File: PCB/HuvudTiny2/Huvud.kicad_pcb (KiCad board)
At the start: 4 copper layers, 42 x 42 mm, 101 parts, among them J1 MOLEX Micro Fit 2x3, J2 DBG, J3 THERM, J4 FAN0, J5 FAN1, J6 Heater, J7 Endstop, J8 THERM, J9 STEPPER, Q1 AO3400A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

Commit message: Remove all traces this time for real.
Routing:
- net HEATER: track 24.9 -> 0.00 mm
- net ENDSTOP2: track 18.3 -> 0.00 mm
- net USBD-: track 16.6 -> 0.00 mm
- net USBD+: track 16.0 -> 0.00 mm
- net /ST_A2: track 14.7 -> 0.00 mm
- net VCC_IO: track 12.9 -> 0.00 mm
- net SDI: track 11.3 -> 0.00 mm
- net /ST_A1: track 10.6 -> 0.00 mm
- net FAN0: track 10.2 -> 0.00 mm
- net /ST_B1: track 9.78 -> 0.00 mm
- net /ST_B2: track 8.28 -> 0.00 mm
- net ENDSTOP1: track 7.13 -> 0.00 mm
- net THERM2: track 5.48 -> 0.00 mm
- net THERM1: track 4.98 -> 0.00 mm
- net NRST: track 3.83 -> 0.00 mm
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
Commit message: Stepper power routed.
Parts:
- moved C9 1.66 mm to (208.0, 129.3), turned to 0 degrees
- turned R24 to 0 degrees
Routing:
- net GND: track 0.00 -> 14.1 mm
- net ST_EN: track 0.00 -> 6.02 mm
- net Net-(C5-Pad1): track 0.00 -> 3.29 mm
- net /ST_B1: track 0.00 -> 3.20 mm
- net Net-(C5-Pad2): track 0.00 -> 2.71 mm
- net /ST_A1: track 0.00 -> 2.68 mm
- net /ST_A2: track 0.00 -> 2.15 mm
- net /ST_B2: track 0.00 -> 1.98 mm
- net Net-(C4-Pad1): track 0.00 -> 1.33 mm
- net BRB: track 0.00 -> 1.20 mm
- net BRA: track 0.00 -> 1.08 mm
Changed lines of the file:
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@@
   )
   (footprint "Capacitor_SMD:C_0402_1005Metric" (layer "F.Cu")
-    (at 206.6 128.4 180)
+    (at 208 129.3)
     (descr "Capacitor SMD 0402 (1005 Metric), square (rectangular) end terminal, IPC_7351 nominal, (Body size source: http://www.tortai-tech.com/upload/download/2011102023233369053.pdf), generated with kicad-footprint-generator")
     (tags "capacitor")
@@
     (fp_line (start -0.5 0.25) (end -0.5 -0.25) (layer "F.Fab") (width 0.1))
     (fp_line (start -0.5 -0.25) (end 0.5 -0.25) (layer "F.Fab") (width 0.1))
-    (pad "1" smd roundrect locked (at -0.485 0 180) (size 0.59 0.64) (layers "F.Cu" "F.Paste" "F.Mask") (roundrect_rratio 0.25)
+    (pad "1" smd roundrect locked (at -0.485 0) (size 0.59 0.64) (layers "F.Cu" "F.Paste" "F.Mask") (roundrect_rratio 0.25)
       (net 2 "GND") (pintype "passive"))
-    (pad "2" smd roundrect locked (at 0.485 0 180) (size 0.59 0.64) (layers "F.Cu" "F.Paste" "F.Mask") (roundrect_rratio 0.25)
+    (pad "2" smd roundrect locked (at 0.485 0) (size 0.59 0.64) (layers "F.Cu" "F.Paste" "F.Mask") (roundrect_rratio 0.25)
       (net 57 "VCC_IO") (pintype "passive"))
     (model "${KISYS3DMOD}/Capacitor_SMD.3dshapes/C_0402_1005Metric.wrl"
@@
   )
   (footprint "Resistor_SMD:R_0402_1005Metric" (layer "F.Cu")
-    (at 206.1 126.4 180)
+    (at 206.1 126.4)
     (descr "Resistor SMD 0402 (1005 Metric), square (rectangular) end terminal, IPC_7351 nominal, (Body size source: http://www.tortai-tech.com/upload/download/2011102023233369053.pdf), generated with kicad-footprint-generator")
     (tags "resistor")
@@
     (fp_line (start 0.5 -0.25) (end 0.5 0.25) (layer "F.Fab") (width 0.1))
     (fp_line (start 0.5 0.25) (end -0.5 0.25) (layer "F.Fab") (width 0.1))
-    (pad "1" smd roundrect locked (at -0.485 0 180) (size 0.59 0.64) (layers "F.Cu" "F.Paste" "F.Mask") (roundrect_rratio 0.25)
+    (pad "1" smd roundrect locked (at -0.485 0) (size 0.59 0.64) (layers "F.Cu" "F.Paste" "F.Mask") (roundrect_rratio 0.25)
       (net 2 "GND") (pintype "passive"))
-    (pad "2" smd roundrect locked (at 0.485 0 180) (size 0.59 0.64) (layers "F.Cu" "F.Paste" "F.Mask") (roundrect_rratio 0.25)
+    (pad "2" smd roundrect locked (at 0.485 0) (size 0.59 0.64) (layers "F.Cu" "F.Paste" "F.Mask") (roundrect_rratio 0.25)
       (net 33 "ST_UART_RX") (pintype "passive"))
     (model "${KISYS3DMOD}/Resistor_SMD.3dshapes/R_0402_1005Metric.wrl"
@@
     (style (thickness 0.15) (arrow_length 1.27) (text_position_mode 2) (extension_height 0.58642) (extension_offset 0) keep_text_aligned)
   )
+  (segment (start 208.8878 124.0878) (end 209.2 124.4) (width 0.2) (layer "F.Cu") (net 2))
+  (segment (start 210.887799 123.1248) (end 210.887799 125.124801) (width 0.2) (layer "F.Cu") (net 2))
+  (segment (start 211.387801 128.1248) (end 211.387801 127.012199) (width 0.2) (layer "F.Cu") (net 2))
+  (segment (start 207.8878 124.624799) (end 208.975201 124.624799) (width 0.2) (layer "F.Cu") (net 2))
+  (segment (start 208.8878 123.1248) (end 208.8878 124.0878) (width 0.2) (layer "F.Cu") (net 2))
+  (segment (start 214.4 128.835) (end 214.4 128.9) (width 0.2) (layer "F.Cu") (net 2))
+  (segment (start 207.8878 126.624801) (end 209.024801 126.624801) (width 0.2) (layer "F.Cu") (net 2))
+  (segment (start 210.887799 125.124801) (end 210.3878 125.6248) (width 0.2) (layer "F.Cu") (net 2))
+  (segment (start 214.4 122.415) (end 214.4 122.1) (width 0.2) (layer "F.Cu") (net 2))
+  (segment (start 207.8878 125.124801) (end 207.8878 124.624799) (width 0.2) (layer "F.Cu") (net 2))
+  (segment (start 214.4 122.1) (end 215.6 120.9) (width 0.2) (layer "F.Cu") (net 2))
+  (segment (start 209.024801 126.624801) (end 209.2 126.8) (width 0.2) (layer "F.Cu") (net 2))
+  (segment (start 208.975201 124.624799) (end 209.2 124.4) (width 0.2) (layer "F.Cu") (net 2))
+  (segment (start 210.3878 126.9122) (end 210.4 126.9) (width 0.2) (layer "F.Cu") (net 2))
+  (segment (start 211.387801 127.012199) (end 211.5 126.9) (width 0.2) (layer "F.Cu") (net 2))
+  (segment (start 214.4 128.9) (end 215.9 130.4) (width 0.2) (layer "F.Cu") (net 2))
+  (segment (start 210.3878 128.1248) (end 210.3878 126.9122) (width 0.2) (layer "F.Cu") (net 2))
   (via (at 209.2 126.8) (size 0.8) (drill 0.4) (layers "F.Cu" "B.Cu") (net 2))
   (via (at 211.5 126.9) (size 0.8) (drill 0.4) (layers "F.Cu" "B.Cu") (net 2))
@@
   (via (at 214.4 131.7) (size 0.8) (drill 0.5) (layers "F.Cu" "B.Cu") (net 3))
   (via (at 213.3 119.5) (size 0.8) (drill 0.5) (layers "F.Cu" "B.Cu") (net 3))
+  (segment (start 206.6602 124.1248) (end 206.585 124.2) (width 0.2) (layer "F.Cu") (net 5))
+  (segment (start 207.8878 124.1248) (end 206.6602 124.1248) (width 0.2) (layer "F.Cu") (net 5))
+  (segment (start 209.887801 122.671827) (end 208.040974 120.825) (width 0.3) (layer "F.Cu") (net 6))
+  (segment (start 209.887801 123.1248) (end 209.887801 122.671827) (width 0.3) (layer "F.Cu") (net 6))
+  (segment (start 208.040974 120.825) (end 207.8125 120.825) (width 0.3) (layer "F.Cu") (net 6))
+  (segment (start 210.3878 123.1248) (end 210.3878 122.568648) (width 0.3) (layer "F.Cu") (net 7))
+  (segment (start 210.3878 122.568648) (end 209.3875 121.568348) (width 0.3) (layer "F.Cu") (net 7))
+  (segment (start 209.3875 121.568348) (end 209.3875 120.825) (width 0.3) (layer "F.Cu") (net 7))
   (via (at 207.99 110.665) (size 0.6) (drill 0.3) (layers "F.Cu" "B.Cu") (net 16))
   (via (at 207.99 111.465) (size 0.6) (drill 0.3) (layers "F.Cu" "B.Cu") (net 16))
   (via (at 206.99 111.465) (size 0.6) (drill 0.3) (layers "F.Cu" "B.Cu") (net 16))
   (via (at 206.99 110.665) (size 0.6) (drill 0.3) (layers "F.Cu" "B.Cu") (net 16))
+  (segment (start 210.8 122.5) (end 210.01502 121.71502) (width 0.127) (layer "F.Cu") (net 18))
+  (segment (start 210.01502 120.31502) (end 209.185 119.485) (width 0.127) (layer "F.Cu") (net 18))
+  (segment (start 209.185 119.485) (end 208 119.485) (width 0.127) (layer "F.Cu") (net 18))
+  (segment (start 210.01502 121.71502) (end 210.01502 120.31502) (width 0.127) (layer "F.Cu") (net 18))
+  (segment (start 211.387801 123.1248) (end 211.387801 122.5978) (width 0.127) (layer "F.Cu") (net 18))
+  (segment (start 211.290001 122.5) (end 210.8 122.5) (width 0.127) (layer "F.Cu") (net 18))
+  (segment (start 211.387801 122.5978) (end 211.290001 122.5) (width 0.127) (layer "F.Cu") (net 18))
+  (segment (start 213.7 126.803178) (end 213.7 127) (width 0.3) (layer "F.Cu") (net 30))
+  (segment (start 213.521623 126.624801) (end 213.7 126.803178) (width 0.3) (layer "F.Cu") (net 30))
+  (segment (start 212.8878 126.624801) (end 213.521623 126.624801) (width 0.3) (layer "F.Cu") (net 30))
+  (segment (start 212.8878 124.624799) (end 213.572023 124.624799) (width 0.3) (layer "F.Cu") (net 31))
+  (segment (start 213.8 124.396822) (end 213.8 124.2) (width 0.3) (layer "F.Cu") (net 31))
+  (segment (start 213.572023 124.624799) (end 213.8 124.396822) (width 0.3) (layer "F.Cu") (net 31))
+  (segment (start 211.8878 128.4878) (end 212.2 128.8) (width 0.4) (layer "F.Cu") (net 40))
+  (segment (start 211.8878 128.1248) (end 211.8878 128.4878) (width 0.4) (layer "F.Cu") (net 40))
   (via (at 211.2 129.6) (size 0.8) (drill 0.4) (layers "F.Cu" "B.Cu") (net 40))
   (via (at 212.2 129.6) (size 0.8) (drill 0.4) (layers "F.Cu" "B.Cu") (net 40))
   (via (at 211.2 130.7) (size 0.8) (drill 0.4) (layers "F.Cu" "B.Cu") (net 40))
   (via (at 212.2 130.7) (size 0.8) (drill 0.4) (layers "F.Cu" "B.Cu") (net 40))
+  (segment (start 218.724 129.476) (end 218.7 129.5) (width 0.8) (layer "B.Cu") (net 40))
+  (segment (start 220.0385 129.476) (end 218.724 129.476) (width 0.8) (layer "B.Cu") (net 40))
+  (segment (start 218.876 126.976) (end 218.8 126.9) (width 0.8) (layer "F.Cu") (net 41))
+  (segment (start 213.624799 126.124799) (end 214.1 126.6) (width 0.3) (layer "F.Cu") (net 41))
+  (segment (start 212.8878 126.124799) (end 213.624799 126.124799) (width 0.3) (layer "F.Cu") (net 41))
+  (segment (start 220.0385 126.976) (end 218.876 126.976) (width 0.8) (layer "F.Cu") (net 41))
+  (segment (start 213.7 125.1) (end 214.1 124.7) (width 0.3) (layer "F.Cu") (net 42))
+  (segment (start 214.1 124.7) (end 214.8 124.7) (width 0.3) (layer "F.Cu") (net 42))
+  (segment (start 220.0385 124.476) (end 218.924 124.476) (width 0.8) (layer "F.Cu") (net 42))
+  (segment (start 212.8878 125.124801) (end 213.675199 125.124801) (width 0.3) (layer "F.Cu") (net 42))
+  (segment (start 213.675199 125.124801) (end 213.7 125.1) (width 0.3) (layer "F.Cu") (net 42))
+  (segment (start 211.8878 123.1248) (end 211.8878 122.8122) (width 0.4) (layer "F.Cu") (net 43))
+  (segment (start 211.8878 122.8122) (end 212.1 122.6) (width 0.4) (layer "F.Cu") (net 43))
   (via (at 212.2 120.7) (size 0.8) (drill 0.4) (layers "F.Cu" "B.Cu") (net 43))
   (via (at 212.2 121.7) (size 0.8) (drill 0.4) (layers "F.Cu" "B.Cu") (net 43))
   (via (at 211.2 120.7) (size 0.8) (drill 0.4) (layers "F.Cu" "B.Cu") (net 43))
   (via (at 211.2 121.7) (size 0.8) (drill 0.4) (layers "F.Cu" "B.Cu") (net 43))
+  (segment (start 220.0385 121.976) (end 218.676 121.976) (width 0.8) (layer "B.Cu") (net 43))
   (zone (net 2) (net_name "GND") (layer "F.Cu") (hatch edge 0.508)
     (priority 5)

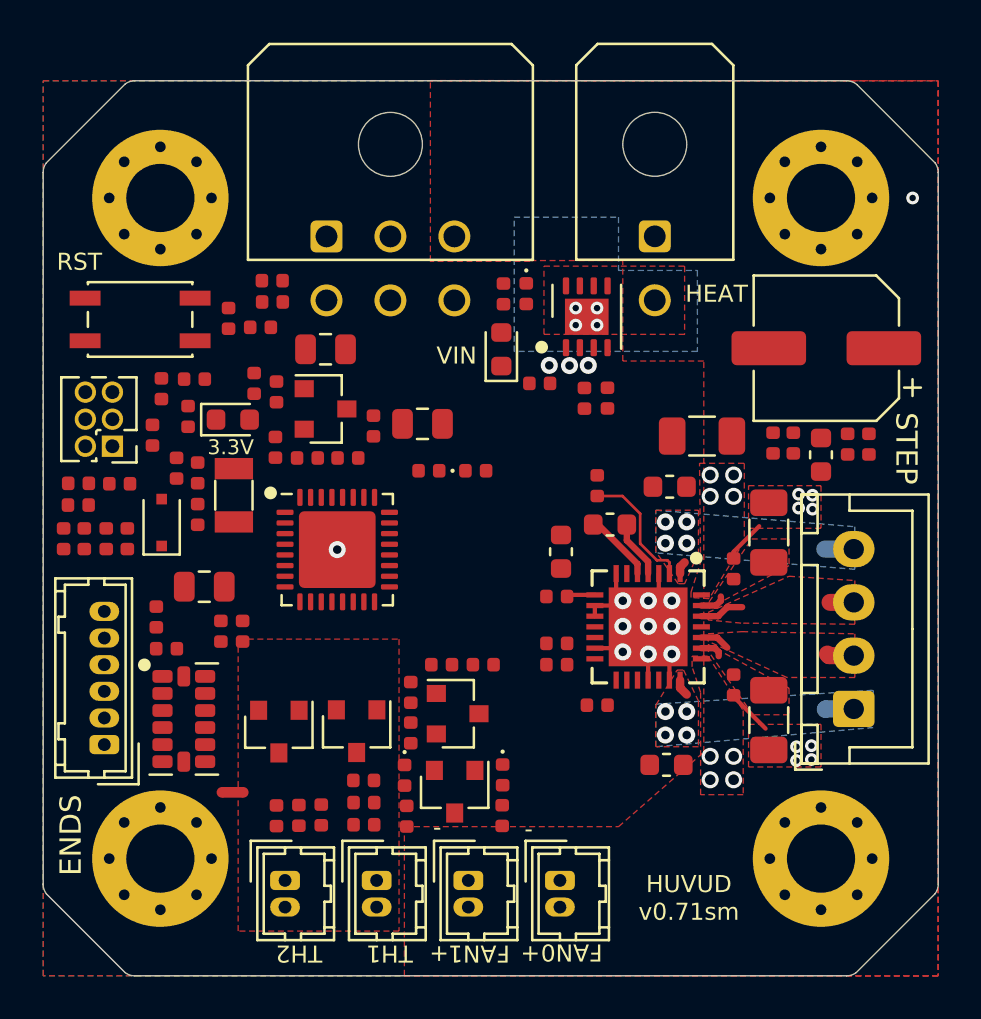
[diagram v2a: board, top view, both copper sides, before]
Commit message: Routed all traces.
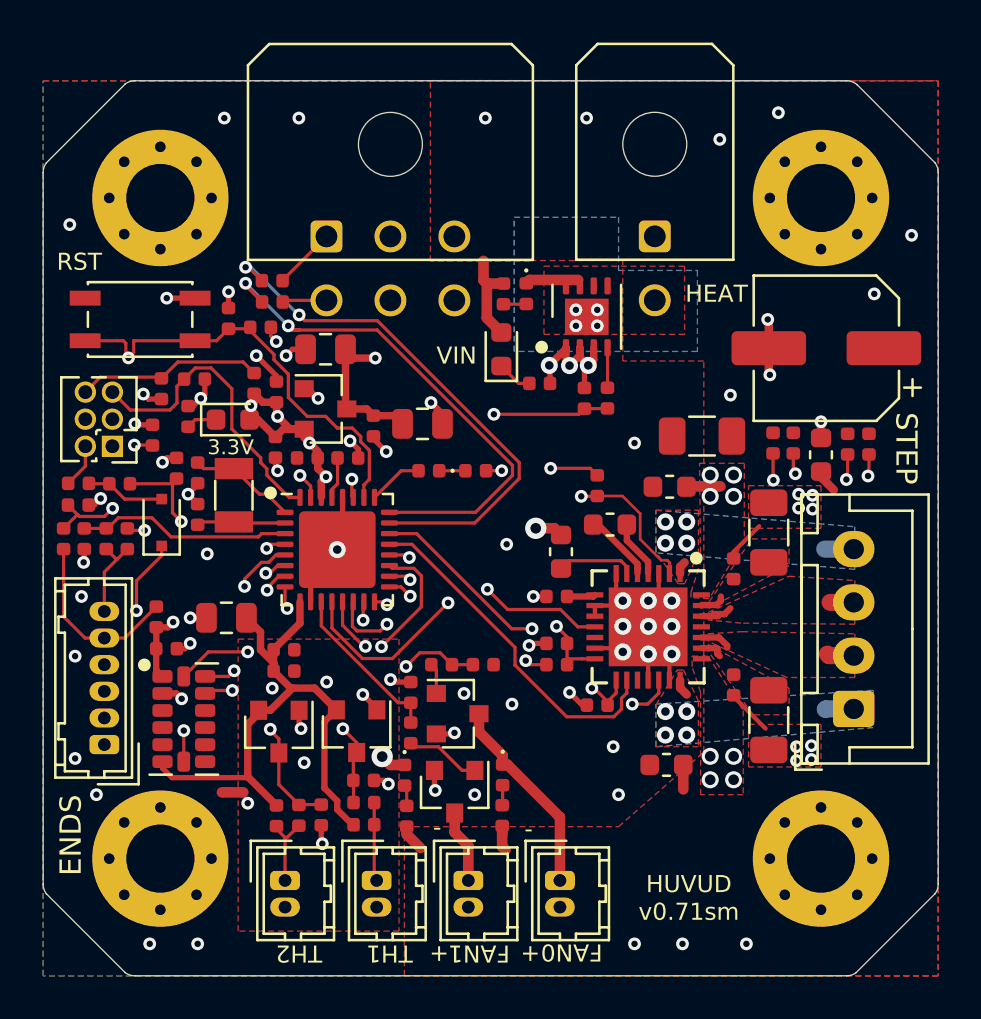
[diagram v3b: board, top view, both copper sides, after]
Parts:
- moved C11 3.50 mm to (193.3, 127.7), turned to 180 degrees
- moved C23 2.13 mm to (193.3, 126.7), turned to 180 degrees
- moved L1 1.79 mm to (190.6, 125.2)
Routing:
- net GND: track 14.1 -> 53.5 mm, vias 21 -> 65
- net ST_VS: track 0.00 -> 32.2 mm, vias 9 -> 19
- net AREF: track 0.00 -> 28.5 mm
- net +3V3: track 0.00 -> 27.6 mm, vias 0 -> 11
- net USBD-: track 0.00 -> 25.4 mm, vias 0 -> 2
- net USBD+: track 0.00 -> 24.5 mm, vias 0 -> 2
- net NRST: track 0.00 -> 23.8 mm, vias 0 -> 1
- net SWCLK: track 0.00 -> 22.4 mm, vias 0 -> 1
- net HEATER: track 0.00 -> 20.7 mm, vias 0 -> 2
- net ST_DIAG: track 0.00 -> 19.7 mm, vias 0 -> 2
- net VCC_IO: track 0.00 -> 19.0 mm, vias 0 -> 2
- net ENDSTOP2: track 0.00 -> 18.8 mm, vias 0 -> 2
- net ST_EN: track 6.02 -> 24.8 mm, vias 0 -> 2
- net ACS: track 0.00 -> 18.2 mm, vias 0 -> 2
- net ST_DIR: track 0.00 -> 16.8 mm, vias 0 -> 2
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
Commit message: Improve layout.
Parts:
- moved D5 2.10 mm to (200.2, 118.2), turned to 180 degrees
- moved R3 1.00 mm to (200.2, 119.3)
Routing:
- net USBD+: track 24.5 -> 21.7 mm
- net USBD-: track 25.4 -> 22.6 mm
- net THERM1: track 13.7 -> 16.4 mm
- net ST_VS: track 32.2 -> 30.0 mm
- net /ST_A2: track 14.8 -> 16.2 mm
- net /ST_B2: track 8.12 -> 9.07 mm
- net BRB: track 1.20 -> 2.02 mm
- net Net-(D1-Pad1): track 9.53 -> 10.2 mm
- net /ST_B1: track 11.4 -> 12.0 mm
- net Net-(D2-Pad1): track 12.2 -> 12.7 mm
- net GNDA: vias 8 -> 7

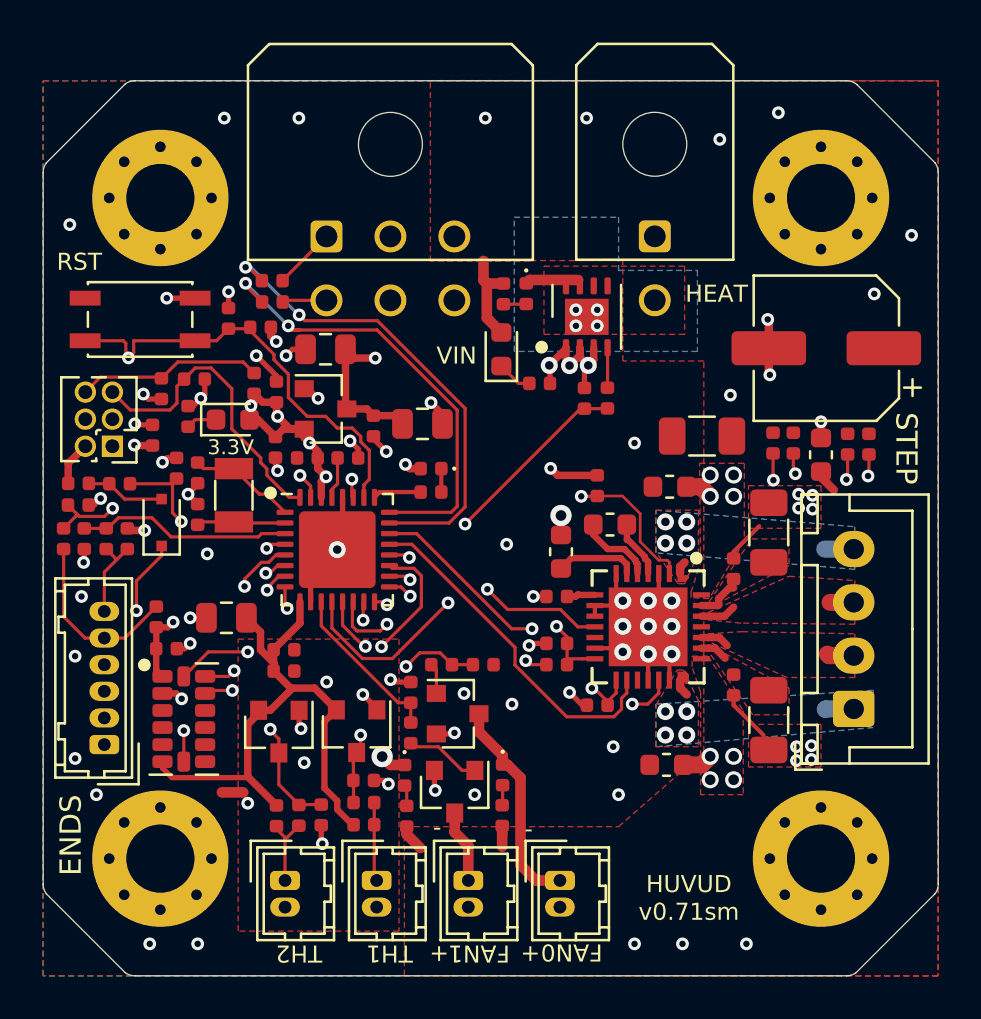
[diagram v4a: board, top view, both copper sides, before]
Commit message: Add third fan mosfet (could be used for lighing).
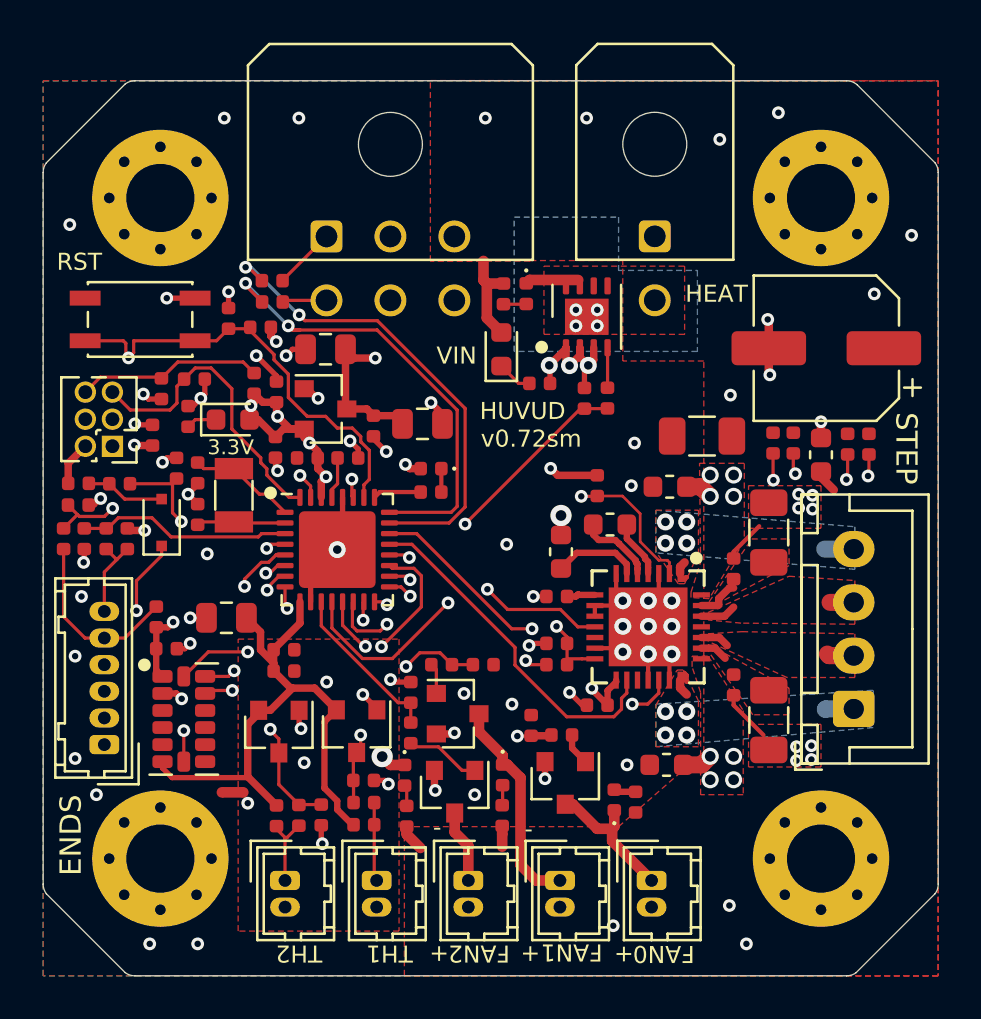
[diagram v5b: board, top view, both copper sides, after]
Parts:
- added D10: LEDGR, LED_SMD:LED_0402_1005Metric, F.Cu at (208.8, 133.8)
- added J10: FAN0, Connector_Hirose:Hirose_DF13-02P-1.25DSA_1x02_P1.25mm_Vertical, F.Cu at (210.6, 137.5)
- added Q4: AO3400A, Package_TO_SOT_SMD:SOT-23, F.Cu at (206.5, 132.9)
- added R23: 10k, Resistor_SMD:R_0402_1005Metric, F.Cu at (204.9, 130.2)
- added R27: 22, Resistor_SMD:R_0402_1005Metric, F.Cu at (206.3, 130.7)
- added R29: 10k, Resistor_SMD:R_0402_1005Metric, F.Cu at (209.8, 133.8)
- J4: value FAN0 -> FAN1
- J5: value FAN1 -> FAN2
- turned R10 to 90 degrees
- turned R12 to 90 degrees
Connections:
- C9 pad 2: VCC_IO -> +3V3
- R10 pad 1: GND -> FAN2
- R10 pad 2: FAN1 -> GND
- R12 pad 1: GND -> HEATER
- R12 pad 2: HEATER -> GND
- R34 pad 1: FAN0 -> FAN1
- R35 pad 1: FAN1 -> FAN2
- R8 pad 2: FAN0 -> FAN1
- U2 pad 15: VCC_IO -> +3V3
- U3 pad 11: FAN1 -> FAN2
- U3 pad 27: VCC_IO -> FAN0
- U3 pad 8: FAN0 -> FAN1
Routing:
- net VCC_IO: track 19.0 -> 0.00 mm, vias 2 -> 0
- net FAN0: track 11.4 -> 19.8 mm
- net FAN2: track 0.00 -> 7.75 mm
- net Net-(D10-Pad1): track 0.00 -> 6.77 mm
- net +3V3: track 27.7 -> 33.3 mm, vias 11 -> 12
- net FAN1: track 7.75 -> 11.4 mm, vias 0 -> 2
- net Net-(Q4-Pad1): track 0.00 -> 1.51 mm
- net Net-(D10-Pad2): track 0.00 -> 1.04 mm
- net GND: track 53.7 -> 54.5 mm, vias 65 -> 66
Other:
- board text added: "(c) iQury.us"
- board text added: "FAN2"
- board text added: "Oct 2021"
- board text added: "v0.72sm"
- board text removed: "v0.71sm"
